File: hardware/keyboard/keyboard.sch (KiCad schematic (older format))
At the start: 1 part

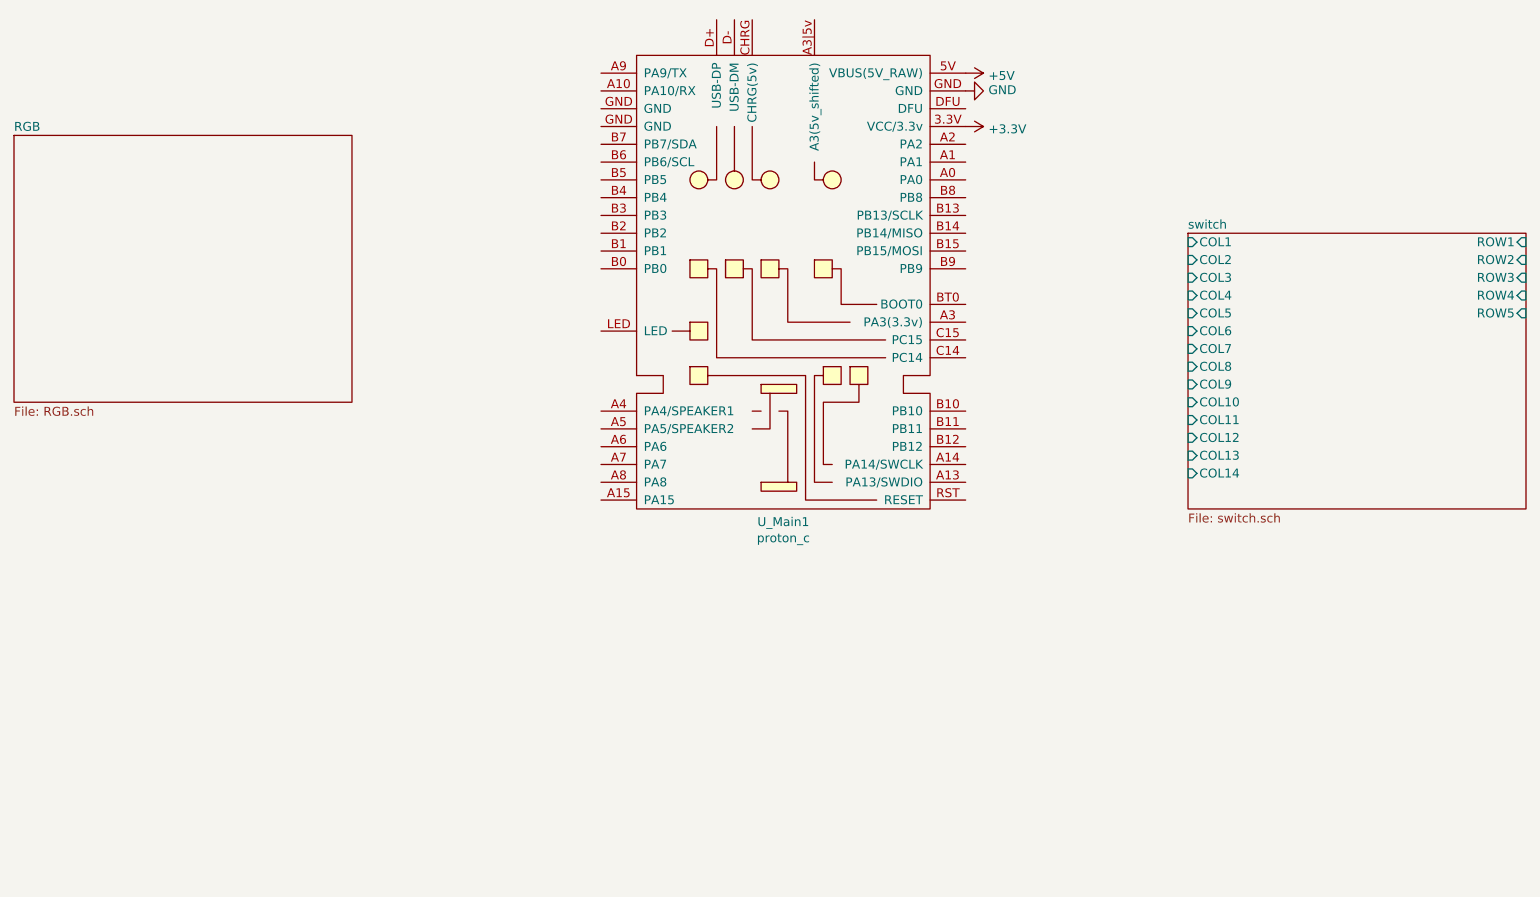
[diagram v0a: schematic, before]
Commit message: switch to proper type of RGB(Common anode)
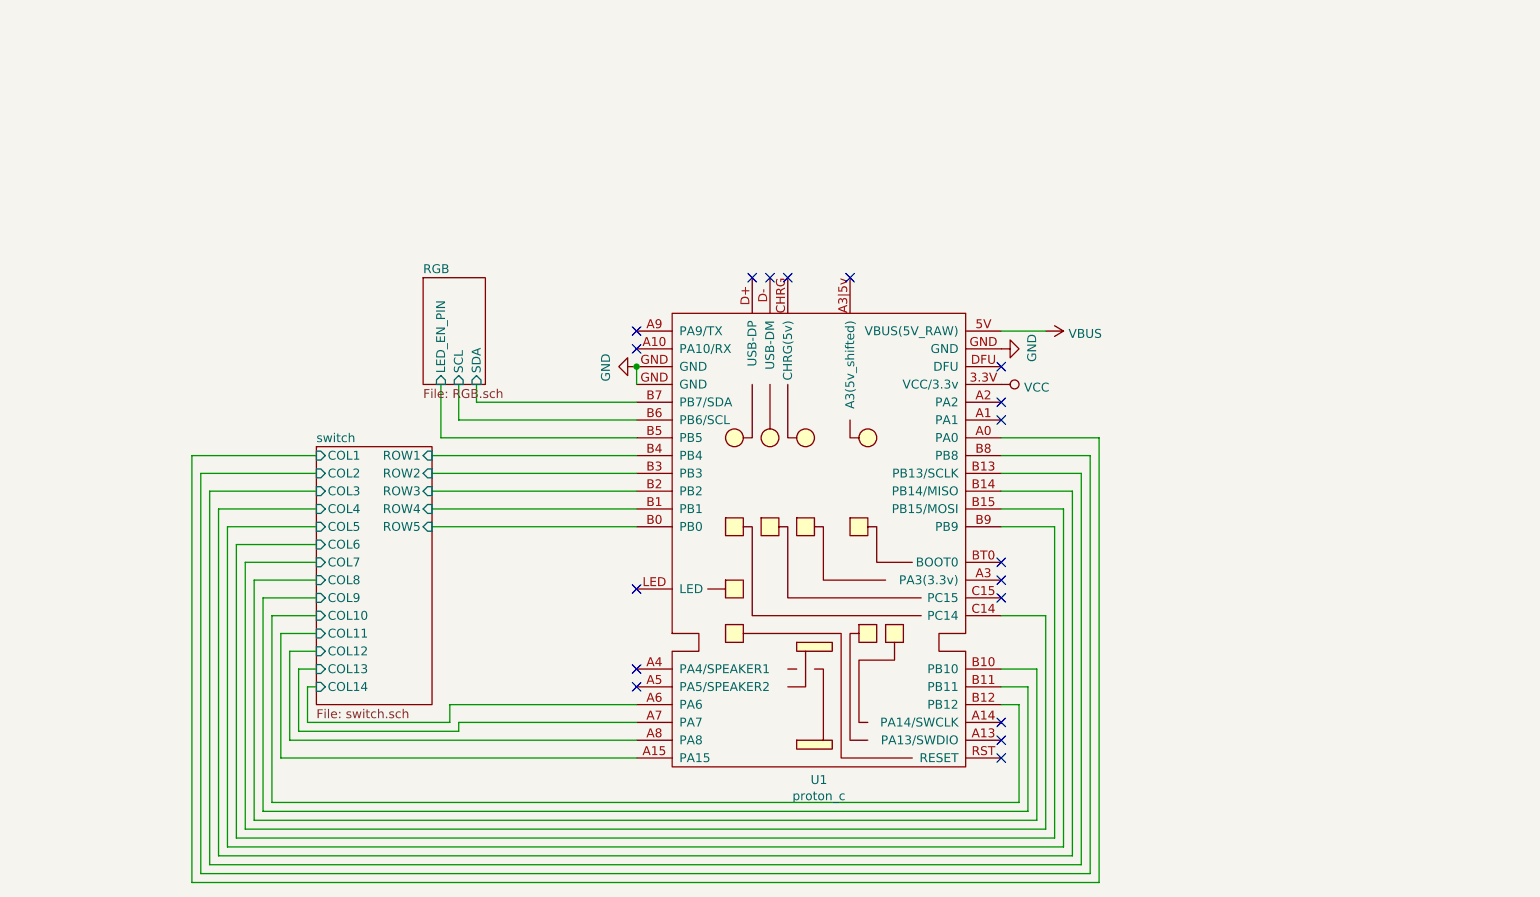
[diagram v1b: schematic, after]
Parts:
- removed U_Main1: proton_c, symbol proton_c:proton_c
- added U1: proton_c, proton_c_eagle:PROTON-C-THT-SPEAKER, symbol proton_c:proton_c
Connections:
- net GND: now also U1.GND
- net switch/COL1: now also U1.A0 (PA0)
- net switch/COL10: now also U1.B12 (PB12)
- net switch/COL11: now also U1.A15 (PA15)
- net switch/COL12: now also U1.A8 (PA8)
- net switch/COL13: now also U1.A7 (PA7)
- net switch/COL14: now also U1.A6 (PA6)
- net switch/COL2: now also U1.B8 (PB8)
- net switch/COL3: now also U1.B13 (PB13/SCLK)
- net switch/COL4: now also U1.B14 (PB14/MISO)
- net switch/COL5: now also U1.B15 (PB15/MOSI)
- net switch/COL6: now also U1.B9 (PB9)
- net switch/COL7: now also U1.C14 (PC14)
- net switch/COL8: now also U1.B10 (PB10)
- net switch/COL9: now also U1.B11 (PB11)
- net switch/ROW1: now also U1.B4 (PB4)
- net switch/ROW2: now also U1.B3 (PB3)
- net switch/ROW3: now also U1.B2 (PB2)
- net switch/ROW4: now also U1.B1 (PB1)
- net switch/ROW5: now also U1.B0 (PB0)
- new net RGB/LED_EN_PIN: U1.B5 (PB5)
- new net RGB/SCL: U1.B6 (PB6/SCL)
- new net RGB/SDA: U1.B7 (PB7/SDA)
- new net VBUS: U1.5V (VBUS(5V_RAW))
- new net VCC: U1.3.3V (VCC/3.3v)
- no-connect marks 0 -> 18

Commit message: use proper footprint, link symbols and footprints
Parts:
- U1: Footprint (none) -> proton_c_eagle:PROTON-C-THT-SPEAKER; Value (none) -> Proton_C
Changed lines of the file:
@@
 F 2 "proton_c_eagle:PROTON-C-THT-SPEAKER" H 6150 3500 50  0001 C CNN
 F 3 "" H 6150 3500 50  0001 C CNN
+F 4 "Proton_C" H 6300 3500 50  0001 C CNN "Value"
+F 5 "proton_c_eagle:PROTON-C-THT-SPEAKER" H 6300 3500 50  0001 C CNN "Footprint"
 	1    6300 3500
 	1    0    0    -1

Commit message: finally the net is kinda working
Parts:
- U1: footprint proton_c_eagle:PROTON-C-THT-SPEAKER -> proton_c:proton_c; Footprint proton_c_eagle:PROTON-C-THT-SPEAKER -> proton_c:proton_c
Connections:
- net switch/COL1: now also U1.A1 (PA1); no longer U1.A0 (PA0)
- net switch/COL2: now also U1.A0 (PA0); no longer U1.B8 (PB8)
- net switch/COL3: now also U1.B8 (PB8); no longer U1.B13 (PB13/SCLK)
- net switch/COL4: now also U1.B13 (PB13/SCLK); no longer U1.B14 (PB14/MISO)
- net switch/COL5: now also U1.B14 (PB14/MISO); no longer U1.B15 (PB15/MOSI)
- net switch/COL6: now also U1.B15 (PB15/MOSI); no longer U1.B9 (PB9)
- net switch/COL7: now also U1.B9 (PB9); no longer U1.C14 (PC14)
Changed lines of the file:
@@
 	3050 5300 7550 5300
-Wire Wire Line
-	7550 5300 7550 4100
-Wire Wire Line
-	7550 4100 7300 4100
-Wire Wire Line
-	7300 3600 7600 3600
-Wire Wire Line
-	7600 3600 7600 5350
 Wire Wire Line
 	7600 5350 3000 5350
@@
 	2950 5400 7650 5400
 Wire Wire Line
-	7650 5400 7650 3500
-Wire Wire Line
-	7650 3500 7300 3500
-Wire Wire Line
-	7300 3400 7700 3400
-Wire Wire Line
-	7700 3400 7700 5450
-Wire Wire Line
 	7700 5450 2900 5450
 Wire Wire Line
@@
 	2850 5500 7750 5500
 Wire Wire Line
-	7750 5500 7750 3300
-Wire Wire Line
-	7750 3300 7300 3300
-Wire Wire Line
-	7300 3200 7800 3200
-Wire Wire Line
-	7800 3200 7800 5550
-Wire Wire Line
 	7800 5550 2800 5550
 Wire Wire Line
@@
 Wire Wire Line
 	2750 5600 7850 5600
-Wire Wire Line
-	7850 5600 7850 3100
-Wire Wire Line
-	7850 3100 7300 3100
-NoConn ~ 7300 3000
 NoConn ~ 7300 3900
 NoConn ~ 7300 4000
@@
 F 0 "U1" H 6275 1977 50  0000 C CNN
 F 1 "proton_c" H 6275 1886 50  0000 C CNN
-F 2 "proton_c_eagle:PROTON-C-THT-SPEAKER" H 6150 3500 50  0001 C CNN
+F 2 "proton_c:proton_c" H 6150 3500 50  0001 C CNN
 F 3 "" H 6150 3500 50  0001 C CNN
 F 4 "Proton_C" H 6300 3500 50  0001 C CNN "Value"
-F 5 "proton_c_eagle:PROTON-C-THT-SPEAKER" H 6300 3500 50  0001 C CNN "Footprint"
+F 5 "proton_c:proton_c" H 6300 3500 50  0001 C CNN "Footprint"
 	1    6300 3500
 	1    0    0    -1
@@
 	0    1    1    0
 $EndComp
+NoConn ~ 7300 4100
+Wire Wire Line
+	7300 3000 7850 3000
+Wire Wire Line
+	7850 3000 7850 5600
+Wire Wire Line
+	7300 3100 7800 3100
+Wire Wire Line
+	7800 3100 7800 5550
+Wire Wire Line
+	7300 3200 7750 3200
+Wire Wire Line
+	7750 3200 7750 5500
+Wire Wire Line
+	7700 5450 7700 3300
+Wire Wire Line
+	7700 3300 7300 3300
+Wire Wire Line
+	7300 3400 7650 3400
+Wire Wire Line
+	7650 3400 7650 5400
+Wire Wire Line
+	7300 3500 7600 3500
+Wire Wire Line
+	7600 3500 7600 5350
+Wire Wire Line
+	7300 3600 7550 3600
+Wire Wire Line
+	7550 3600 7550 5300
 $EndSCHEMATC
